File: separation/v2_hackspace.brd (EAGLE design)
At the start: 40.6 x 25.4 mm, 16 parts

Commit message: ripup all signals
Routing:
- net VSENSE: track 47.8 -> 0.00 mm
- net VCC: track 33.2 -> 0.00 mm
- net SCL: track 18.5 -> 0.00 mm
- net SDA: track 16.3 -> 0.00 mm
- net SERVO: track 15.9 -> 0.00 mm
- net BUZZ: track 12.0 -> 0.00 mm
- net GND: track 5.33 -> 0.00 mm
- net VBAT: track 5.13 -> 0.00 mm
- net A0: track 1.80 -> 0.00 mm
- net TX: track 1.80 -> 0.00 mm
- net SCK: track 1.80 -> 0.00 mm
- net RX: track 1.80 -> 0.00 mm
- net MOSI: track 1.80 -> 0.00 mm
- net A3: track 1.80 -> 0.00 mm
- net +3V3: track 1.80 -> 0.00 mm
- removed copper zone on layer 16, net GND
- removed copper zone on layer 1, net VBAT
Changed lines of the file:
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@@
 <contactref element="R2" pad="2"/>
 <contactref element="SERCON" pad="1"/>
-<wire x1="7.62" y1="17.9705" x2="9.3345" y2="17.9705" width="1.524" layer="1"/>
-<wire x1="9.3345" y1="17.9705" x2="9.398" y2="17.907" width="1.524" layer="1"/>
 <contactref element="LDO" pad="2"/>
 <contactref element="JP1" pad="1"/>
-<wire x1="17.653" y1="17.399" x2="14.468" y2="17.399" width="1.016" layer="1"/>
-<wire x1="14.468" y1="17.399" x2="14.224" y2="17.155" width="1.016" layer="1"/>
-<polygon width="0.254" layer="16" isolate="0.254">
-<vertex x="-22.86" y="-2.54"/>
-<vertex x="20.32" y="-2.54"/>
-<vertex x="22.86" y="0"/>
-<vertex x="22.86" y="25.4"/>
-<vertex x="20.32" y="27.94"/>
-<vertex x="-20.32" y="27.94"/>
-<vertex x="-24.13" y="24.13"/>
-<vertex x="-24.13" y="21.59"/>
-<vertex x="-24.13" y="1.27"/>
-<vertex x="-24.13" y="-1.27"/>
-</polygon>
 <contactref element="C1" pad="1"/>
 <contactref element="C2" pad="1"/>
+<wire x1="14.224" y1="17.155" x2="17.653" y2="17.399" width="0" layer="19" extent="1-1"/>
+<wire x1="7.62" y1="17.9705" x2="14.224" y2="17.155" width="0" layer="19" extent="1-1"/>
+<wire x1="17.335" y1="6.35" x2="17.653" y2="17.399" width="0" layer="19" extent="1-1"/>
+<wire x1="9.915025" y1="3.184025" x2="17.335" y2="6.35" width="0" layer="19" extent="1-1"/>
+<wire x1="-12.192" y1="16.891" x2="7.62" y2="17.9705" width="0" layer="19" extent="1-1"/>
+<wire x1="-14.859" y1="16.891" x2="-12.192" y2="16.891" width="0" layer="19" extent="1-1"/>
+<wire x1="-15.113" y1="12.136" x2="-14.859" y2="16.891" width="0" layer="19" extent="1-1"/>
+<wire x1="-17.526" y1="3.556" x2="-15.113" y2="12.136" width="0" layer="19" extent="1-1"/>
 </signal>
 <signal name="MOSI">
 <contactref element="MCU-R" pad="4"/>
-<wire x1="7.62" y1="12.8905" x2="9.3345" y2="12.8905" width="1.524" layer="1"/>
-<wire x1="9.3345" y1="12.8905" x2="9.398" y2="12.827" width="1.524" layer="1"/>
 </signal>
 <signal name="SCK">
 <contactref element="MCU-R" pad="2"/>
-<wire x1="7.62" y1="7.8105" x2="9.3345" y2="7.8105" width="1.524" layer="1"/>
-<wire x1="9.3345" y1="7.8105" x2="9.398" y2="7.747" width="1.524" layer="1"/>
 </signal>
 <signal name="A3">
 <contactref element="MCU-L" pad="4"/>
-<wire x1="-7.62" y1="12.8905" x2="-9.3345" y2="12.8905" width="1.524" layer="1"/>
-<wire x1="-9.3345" y1="12.8905" x2="-9.398" y2="12.827" width="1.524" layer="1"/>
 </signal>
 <signal name="SDA">
 <contactref element="MCU-L" pad="5"/>
-<wire x1="-7.62" y1="10.3505" x2="-9.3345" y2="10.3505" width="1.524" layer="1"/>
-<wire x1="-9.3345" y1="10.3505" x2="-9.398" y2="10.287" width="1.524" layer="1"/>
 <contactref element="JP2" pad="1"/>
-<wire x1="-17.78" y1="19.05" x2="-16.51" y2="17.78" width="0.508" layer="16"/>
-<wire x1="-16.51" y1="17.78" x2="-16.51" y2="16.51" width="0.508" layer="16"/>
-<wire x1="-10.3505" y1="10.3505" x2="-7.62" y2="10.3505" width="0.508" layer="16"/>
-<wire x1="-16.51" y1="16.51" x2="-10.3505" y2="10.3505" width="0.508" layer="16"/>
+<wire x1="-17.78" y1="19.05" x2="-7.62" y2="10.3505" width="0" layer="19" extent="1-1"/>
 </signal>
 <signal name="SCL">
 <contactref element="MCU-L" pad="6"/>
-<wire x1="-7.62" y1="7.8105" x2="-9.3345" y2="7.8105" width="1.524" layer="1"/>
-<wire x1="-9.3345" y1="7.8105" x2="-9.398" y2="7.747" width="1.524" layer="1"/>
 <contactref element="JP3" pad="1"/>
-<wire x1="-11.6205" y1="7.8105" x2="-7.62" y2="7.8105" width="0.508" layer="16"/>
-<wire x1="-13.97" y1="10.16" x2="-11.6205" y2="7.8105" width="0.508" layer="16"/>
-<wire x1="-17.78" y1="11.43" x2="-17.78" y2="16.51" width="0.508" layer="16"/>
-<wire x1="-13.97" y1="10.16" x2="-16.51" y2="10.16" width="0.508" layer="16"/>
-<wire x1="-16.51" y1="10.16" x2="-17.78" y2="11.43" width="0.508" layer="16"/>
+<wire x1="-7.62" y1="7.8105" x2="-17.78" y2="16.51" width="0" layer="19" extent="1-1"/>
 </signal>
 <signal name="VCC" class="1">
@@
 <contactref element="LDO" pad="3"/>
 <contactref element="JP4" pad="1"/>
-<wire x1="17.653" y1="19.939" x2="14.458" y2="19.939" width="1.016" layer="1"/>
-<wire x1="14.458" y1="19.939" x2="14.224" y2="19.705" width="0.508" layer="1"/>
-<wire x1="13.4185" y1="20.5105" x2="14.224" y2="19.705" width="1.524" layer="1"/>
-<wire x1="7.62" y1="20.5105" x2="13.4185" y2="20.5105" width="1.524" layer="1"/>
 <contactref element="C1" pad="2"/>
-<wire x1="7.62" y1="20.5105" x2="4.8895" y2="20.5105" width="0.508" layer="1"/>
-<wire x1="-12.192" y1="20.32" x2="-12.192" y2="19.431" width="0.508" layer="1"/>
-<wire x1="4.8895" y1="20.5105" x2="2.54" y2="22.86" width="0.508" layer="1"/>
-<wire x1="2.54" y1="22.86" x2="-9.652" y2="22.86" width="0.508" layer="1"/>
-<wire x1="-9.652" y1="22.86" x2="-12.192" y2="20.32" width="0.508" layer="1"/>
+<wire x1="14.224" y1="19.705" x2="17.653" y2="19.939" width="0" layer="19" extent="1-1"/>
+<wire x1="7.62" y1="20.5105" x2="14.224" y2="19.705" width="0" layer="19" extent="1-1"/>
+<wire x1="-12.192" y1="19.431" x2="7.62" y2="20.5105" width="0" layer="19" extent="1-1"/>
 </signal>
 <signal name="+3V3">
 <contactref element="MCU-R" pad="5"/>
-<wire x1="7.62" y1="15.4305" x2="9.3345" y2="15.4305" width="1.524" layer="1"/>
-<wire x1="9.3345" y1="15.4305" x2="9.398" y2="15.367" width="1.524" layer="1"/>
 </signal>
 <signal name="PB22/I6/SERCOM5.3">
@@
 <signal name="TX">
 <contactref element="MCU-L" pad="7"/>
-<wire x1="-7.62" y1="5.2705" x2="-9.3345" y2="5.2705" width="1.524" layer="1"/>
-<wire x1="-9.3345" y1="5.2705" x2="-9.398" y2="5.207" width="1.524" layer="1"/>
 </signal>
 <signal name="RX">
 <contactref element="MCU-R" pad="1"/>
-<wire x1="7.62" y1="5.2705" x2="9.3345" y2="5.2705" width="1.524" layer="1"/>
-<wire x1="9.3345" y1="5.2705" x2="9.398" y2="5.207" width="1.524" layer="1"/>
 </signal>
 <signal name="VBAT">
@@
 <contactref element="R1" pad="1"/>
 <contactref element="SERCON" pad="2"/>
-<wire x1="-14.986" y1="3.556" x2="-14.986" y2="8.509" width="2.032" layer="16"/>
-<wire x1="-14.986" y1="8.509" x2="-15.113" y2="8.636" width="2.032" layer="16"/>
-<polygon width="0.254" layer="1" isolate="0.254">
-<vertex x="-21.59" y="27.94"/>
-<vertex x="21.59" y="27.94"/>
-<vertex x="22.86" y="26.67"/>
-<vertex x="22.86" y="-2.54"/>
-<vertex x="-22.86" y="-2.54"/>
-<vertex x="-24.13" y="-1.27"/>
-<vertex x="-24.13" y="25.4"/>
-</polygon>
 <contactref element="C2" pad="2"/>
+<wire x1="-9.661025" y1="3.184025" x2="14.224" y2="14.605" width="0" layer="19" extent="1-1"/>
+<wire x1="-14.986" y1="3.556" x2="-9.661025" y2="3.184025" width="0" layer="19" extent="1-1"/>
+<wire x1="-15.113" y1="8.636" x2="-14.986" y2="3.556" width="0" layer="19" extent="1-1"/>
+<wire x1="-14.859" y1="19.431" x2="-15.113" y2="8.636" width="0" layer="19" extent="1-1"/>
 </signal>
 <signal name="SERVO">
 <contactref element="SERCON" pad="3"/>
 <contactref element="MCU-L" pad="3"/>
-<wire x1="-11.1125" y1="15.4305" x2="-12.446" y2="14.097" width="0.508" layer="1"/>
-<wire x1="-9.398" y1="15.4305" x2="-11.1125" y2="15.4305" width="0.508" layer="1"/>
-<wire x1="-12.446" y1="14.097" x2="-12.446" y2="3.556" width="0.508" layer="1"/>
-<wire x1="-7.62" y1="15.4305" x2="-9.398" y2="15.4305" width="1.524" layer="1"/>
+<wire x1="-7.62" y1="15.4305" x2="-12.446" y2="3.556" width="0" layer="19" extent="1-1"/>
 </signal>
 <signal name="BUZZ">
 <contactref element="LOUD" pad="1"/>
 <contactref element="MCU-R" pad="3"/>
-<wire x1="13.335" y1="6.35" x2="13.335" y2="8.255" width="0.508" layer="1"/>
-<wire x1="11.2395" y1="10.3505" x2="9.398" y2="10.3505" width="0.508" layer="1"/>
-<wire x1="13.335" y1="8.255" x2="11.2395" y2="10.3505" width="0.508" layer="1"/>
-<wire x1="7.62" y1="10.3505" x2="9.398" y2="10.3505" width="1.524" layer="1"/>
 <contactref element="TP6" pad="TP"/>
-<wire x1="15.367" y1="9.017" x2="15.367" y2="8.89" width="0.254" layer="16"/>
-<wire x1="13.335" y1="6.35" x2="15.367" y2="8.382" width="1.016" layer="16"/>
-<wire x1="15.367" y1="8.382" x2="15.367" y2="8.89" width="1.016" layer="16"/>
+<wire x1="13.335" y1="6.35" x2="15.367" y2="9.017" width="0" layer="19" extent="16-16"/>
+<wire x1="7.62" y1="10.3505" x2="13.335" y2="6.35" width="0" layer="19" extent="1-1"/>
 </signal>
 <signal name="VSENSE">
@@
 <contactref element="R2" pad="1"/>
 <contactref element="MCU-L" pad="2"/>
-<wire x1="-7.62" y1="17.9705" x2="-9.398" y2="17.9705" width="1.524" layer="1"/>
 <contactref element="TP2" pad="TP"/>
-<wire x1="-9.271" y1="22.987" x2="-6.477" y2="22.987" width="0.508" layer="16"/>
-<wire x1="-6.477" y1="22.987" x2="-5.08" y2="21.59" width="0.508" layer="16"/>
-<wire x1="-5.08" y1="21.59" x2="-5.08" y2="19.05" width="0.508" layer="16"/>
-<wire x1="-5.08" y1="19.05" x2="-6.35" y2="17.78" width="0.508" layer="16"/>
-<wire x1="-6.35" y1="17.78" x2="-7.4295" y2="17.78" width="0.254" layer="16"/>
-<wire x1="-7.4295" y1="17.78" x2="-7.62" y2="17.9705" width="0.254" layer="16"/>
-<wire x1="-7.864971875" y1="1.387971875" x2="-3.81" y2="1.387971875" width="0.508" layer="1"/>
-<wire x1="-3.81" y1="1.387971875" x2="8.118971875" y2="1.387971875" width="0.508" layer="1"/>
-<wire x1="-3.81" y1="1.387971875" x2="-3.81" y2="16.51" width="0.508" layer="1"/>
-<wire x1="-3.81" y1="16.51" x2="-5.2705" y2="17.9705" width="0.508" layer="1"/>
-<wire x1="-5.2705" y1="17.9705" x2="-7.62" y2="17.9705" width="0.508" layer="1"/>
+<wire x1="-7.62" y1="17.9705" x2="-9.271" y2="22.987" width="0" layer="19" extent="16-16"/>
+<wire x1="-7.864971875" y1="1.387971875" x2="-7.62" y2="17.9705" width="0" layer="19" extent="1-1"/>
+<wire x1="8.118971875" y1="1.387971875" x2="-7.864971875" y2="1.387971875" width="0" layer="19" extent="1-1"/>
 </signal>
 <signal name="A0">
 <contactref element="MCU-L" pad="1"/>
-<wire x1="-7.62" y1="20.5105" x2="-9.3345" y2="20.5105" width="1.524" layer="1"/>
-<wire x1="-9.3345" y1="20.5105" x2="-9.398" y2="20.574" width="1.524" layer="1"/>
 </signal>
 </signals>

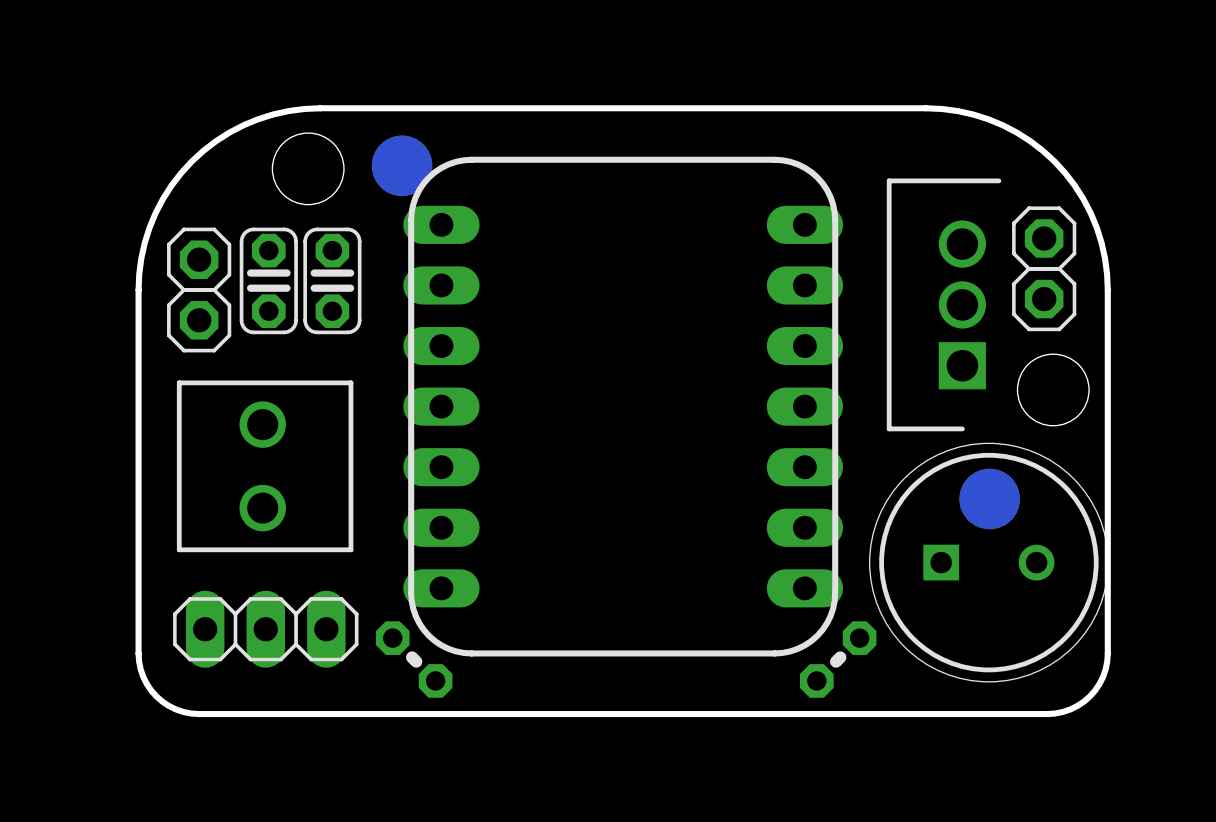
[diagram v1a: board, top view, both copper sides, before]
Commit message: remove testpoints
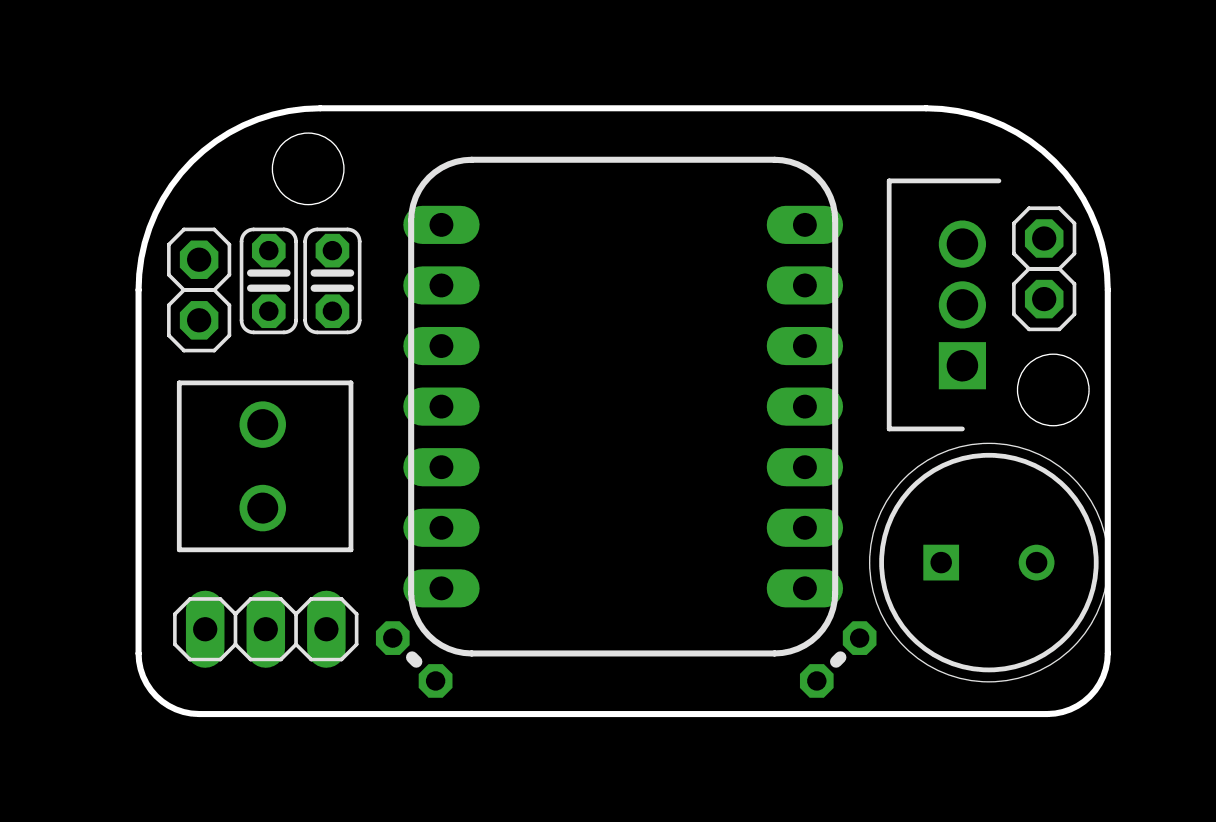
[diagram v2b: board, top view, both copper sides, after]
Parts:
- removed TP2, TP6: TPSQB2,54, testpad:B2,54
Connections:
- net BUZZ: no longer TP6.TP
- net VSENSE: no longer TP2.TP
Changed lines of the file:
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@@
 <attribute name="SPICEPREFIX" value="R" x="9.017" y="2.286" size="1.778" layer="27" font="vector" ratio="15" rot="R45" display="off"/>
-</element>
-<element name="TP2" library="testpad" library_urn="urn:adsk.eagle:library:385" package="B2,54" package3d_urn="urn:adsk.eagle:package:27948/1" value="TPSQB2,54" x="-9.271" y="22.987" smashed="yes" rot="MR0">
-<attribute name="POPULARITY" value="0" x="-9.271" y="22.987" size="0.8382" layer="28" font="vector" rot="MR0" display="off"/>
-<attribute name="TP_SIGNAL_NAME" value="" x="-9.271" y="22.987" size="0.8382" layer="28" font="vector" rot="MR0" display="off"/>
-<attribute name="VALUE" x="-8.001" y="21.59" size="0.0254" layer="28" rot="MR0"/>
-</element>
-<element name="TP6" library="testpad" library_urn="urn:adsk.eagle:library:385" package="B2,54" package3d_urn="urn:adsk.eagle:package:27948/1" value="TPSQB2,54" x="15.367" y="9.017" smashed="yes" rot="MR0">
-<attribute name="POPULARITY" value="0" x="15.367" y="9.017" size="0.8382" layer="28" font="vector" rot="MR0" display="off"/>
-<attribute name="TP_SIGNAL_NAME" value="" x="15.367" y="9.017" size="0.8382" layer="28" font="vector" rot="MR0" display="off"/>
-<attribute name="VALUE" x="16.637" y="7.62" size="0.0254" layer="28" rot="MR0"/>
 </element>
 <element name="JP2" library="pinhead" library_urn="urn:adsk.eagle:library:325" package="1X01" package3d_urn="urn:adsk.eagle:package:22485/2" value="" x="-17.78" y="19.05" smashed="yes">
@@
 <contactref element="LOUD" pad="1"/>
 <contactref element="MCU-R" pad="3"/>
-<contactref element="TP6" pad="TP"/>
-<wire x1="13.335" y1="6.35" x2="15.367" y2="9.017" width="0" layer="19" extent="16-16"/>
 <wire x1="7.62" y1="10.3505" x2="13.335" y2="6.35" width="0" layer="19" extent="1-1"/>
 </signal>
@@
 <contactref element="R2" pad="1"/>
 <contactref element="MCU-L" pad="2"/>
-<contactref element="TP2" pad="TP"/>
-<wire x1="-7.62" y1="17.9705" x2="-9.271" y2="22.987" width="0" layer="19" extent="16-16"/>
 <wire x1="-7.864971875" y1="1.387971875" x2="-7.62" y2="17.9705" width="0" layer="19" extent="1-1"/>
 <wire x1="8.118971875" y1="1.387971875" x2="-7.864971875" y2="1.387971875" width="0" layer="19" extent="1-1"/>
